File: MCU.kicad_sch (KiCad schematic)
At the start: 48 parts, among them IC3 TCAN330DCNT, J1 BM04B-GHS-TBT_LF__SN__N_, J2 Conn_01x04_Pin, J3 USB_C_Receptacle_USB2.0_16P, J4 BM04B-GHS-TBT_LF__SN__N_, J5 Conn_01x02_Socket, SW1 SW_SPDT, SW2 SW_SPDT, U2 STM32G431CBU6, U3 ME6211C33M5, Y1 ECS-80-20-5PX-TR

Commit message: all routed pcb
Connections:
- net I2C1_SCL: no longer J4.3, R22.2, U2.45 (PB7)
- new net I2C1_SDA: J4.3, R22.2, U2.45 (PB7)
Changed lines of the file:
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@@
-	)
-	(junction
-		(at 68.58 60.96)
-		(diameter 0)
-		(color 0 0 0 0)
 	)
 	(junction
@@
 	(wire
 		(pts
-			(xy 68.58 60.96) (xy 71.12 60.96)
+			(xy 45.72 60.96) (xy 71.12 60.96)
 		)
 		(stroke
@@
 		)
 		(stroke
-			(width 0)
-			(type default)
-		)
-	)
-	(wire
-		(pts
-			(xy 45.72 60.96) (xy 68.58 60.96)
-		)
-		(stroke

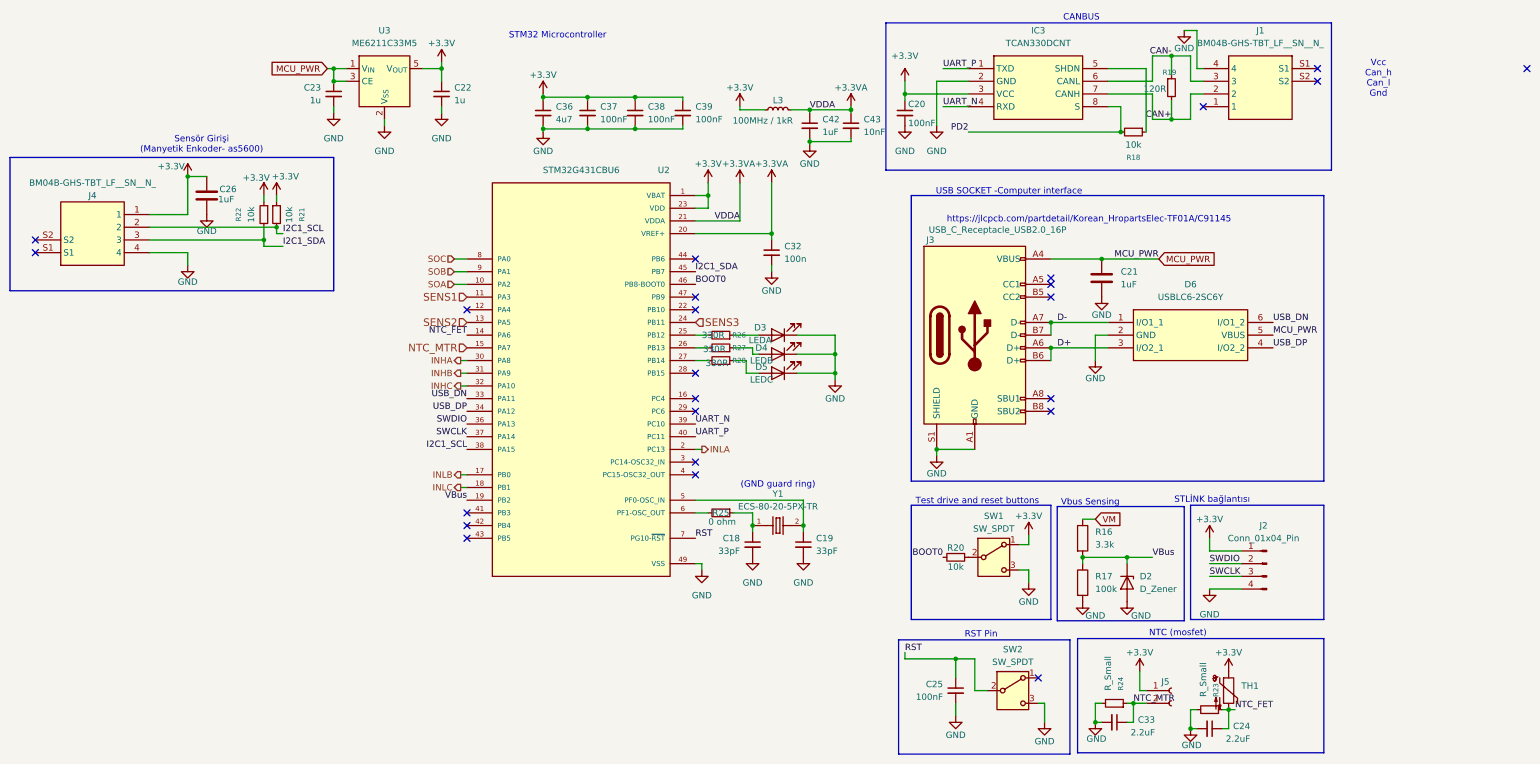
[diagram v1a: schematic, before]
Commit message: New one_GND_Layer pcb desgin has finished yet. DRC Rule checks needs to be controlling and correcting still.
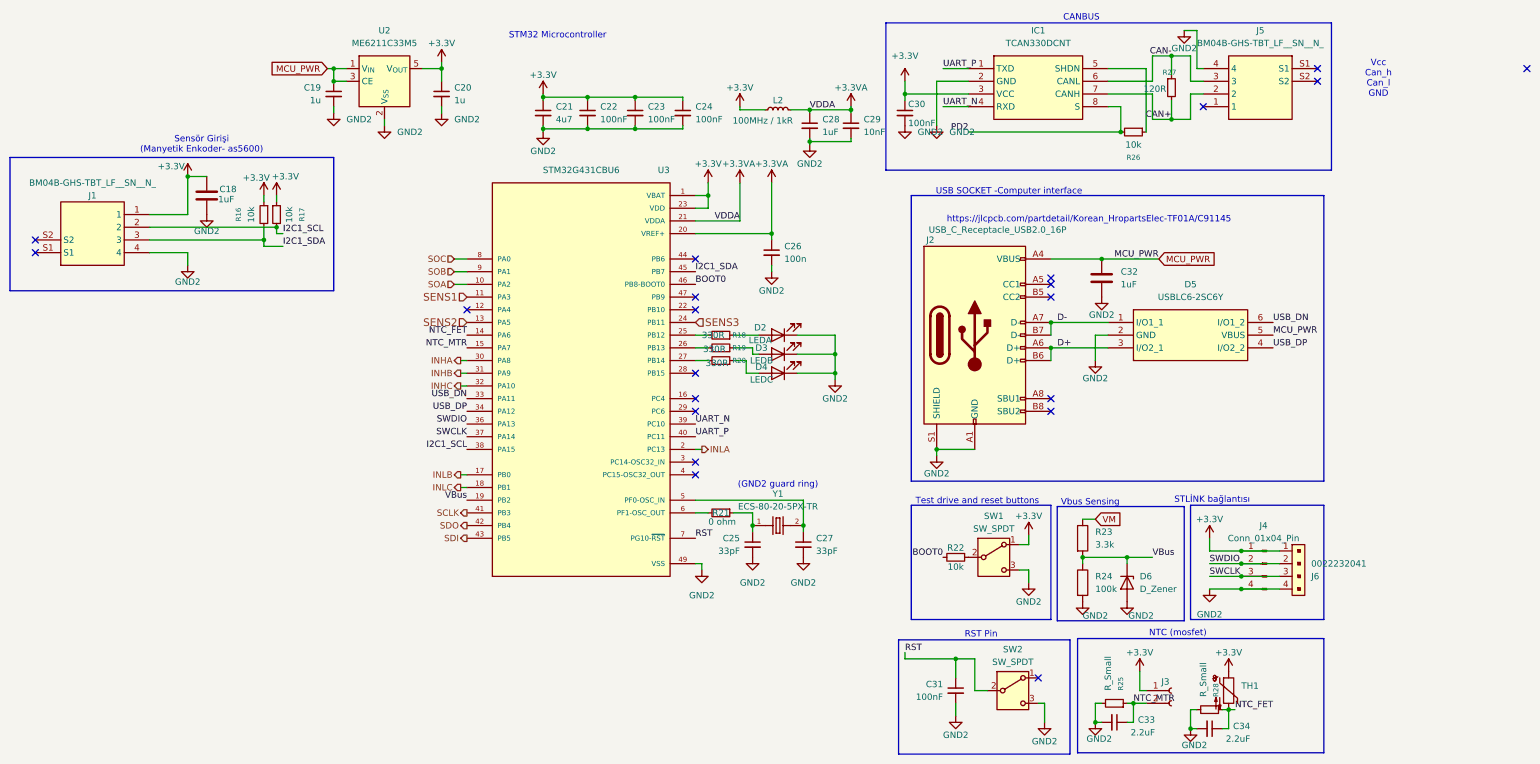
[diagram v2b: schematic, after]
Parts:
- added J6: 0022232041, digikey-footprints:PinHeader_1x4_P2.54mm_Drill1.02mm, symbol dk_Rectangular-Connectors-Headers-Male-Pins:0022232041
- renumbered C26 to C18, C23 to C19, C22 to C20, C36 to C21, C37 to C22, C38 to C23, C39 to C24, C18 to C25, C32 to C26, C19 to C27, C42 to C28, C43 to C29, C20 to C30, C25 to C31, C21 to C32, C24 to C34, D3 to D2, D4 to D3, D5 to D4, D6 to D5, D2 to D6, IC3 to IC1, J4 to J1, J3 to J2, J5 to J3, J2 to J4, J1 to J5, L3 to L2, R22 to R16, R21 to R17, R26 to R18, R27 to R19, R28 to R20, R25 to R21, R20 to R22, R16 to R23, R17 to R24, R24 to R25, R18 to R26, R19 to R27, R23 to R28, U3 to U2, U2 to U3
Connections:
- net +3.3V: now also J6.1
- net SWCLK: now also J6.3
- net SWDIO: now also J6.2
- net SCLK: now reaches U3.41 (PB3)
- net SDO: now reaches U3.42 (PB4)
- net SDI: now reaches U3.43 (PB5)
- net GND renamed GND2
- net GND2: now also J6.4
- no-connect marks 24 -> 21
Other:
- note added: "(GND2 guard ring)"
- note added: "Vcc Can_h Can_l GND"
- note removed: "(GND guard ring)"
- note removed: "Vcc Can_h Can_l Gnd"

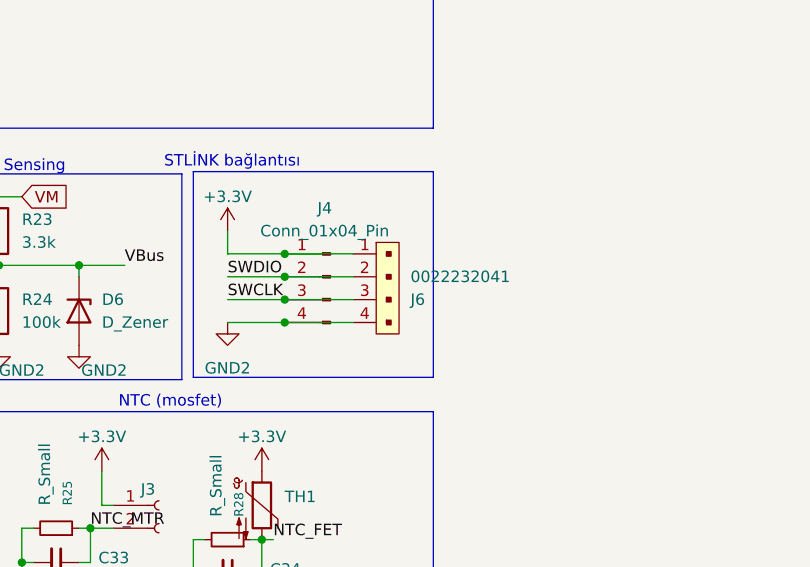
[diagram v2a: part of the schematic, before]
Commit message: some drc rule checks and correcting
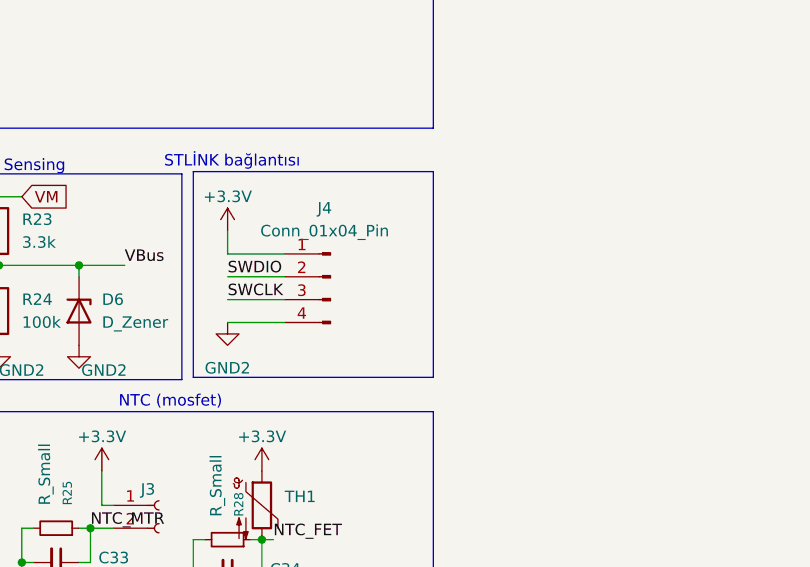
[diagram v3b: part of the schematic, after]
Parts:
- removed J6: 0022232041, digikey-footprints:PinHeader_1x4_P2.54mm_Drill1.02mm, symbol dk_Rectangular-Connectors-Headers-Male-Pins:0022232041
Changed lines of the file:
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@@
 	)
 	(junction
-		(at 264.16 125.73)
-		(diameter 0)
-		(color 0 0 0 0)
-	)
-	(junction
 		(at 196.85 34.29)
 		(diameter 0)
@@
 	)
 	(junction
-		(at 264.16 133.35)
-		(diameter 0)
-		(color 0 0 0 0)
-	)
-	(junction
 		(at 133.35 41.275)
 		(diameter 0)
@@
 	)
 	(junction
-		(at 264.16 130.81)
-		(diameter 0)
-		(color 0 0 0 0)
-	)
-	(junction
-		(at 264.16 128.27)
-		(diameter 0)
-		(color 0 0 0 0)
-	)
-	(junction
 		(at 166.37 120.65)
 		(diameter 0)
@@
 	(wire
 		(pts
-			(xy 264.16 133.35) (xy 271.78 133.35)
-		)
-		(stroke
-			(width 0)
-			(type default)
-		)
-	)
-	(wire
-		(pts
 			(xy 234.95 82.55) (xy 234.95 87.63)
 		)
@@
 	(wire
 		(pts
-			(xy 264.16 125.73) (xy 271.78 125.73)
-		)
-		(stroke
-			(width 0)
-			(type default)
-		)
-	)
-	(wire
-		(pts
 			(xy 170.18 62.23) (xy 170.18 63.5)
 		)
@@
 	(wire
 		(pts
-			(xy 264.16 128.27) (xy 271.78 128.27)
-		)
-		(stroke
-			(width 0)
-			(type default)
-		)
-	)
-	(wire
-		(pts
 			(xy 224.79 160.02) (xy 224.79 156.21)
 		)
@@
 	(wire
 		(pts
-			(xy 264.16 130.81) (xy 271.78 130.81)
-		)
-		(stroke
-			(width 0)
-			(type default)
-		)
-	)
-	(wire
-		(pts
 			(xy 124.46 41.275) (xy 133.35 41.275)
 		)
@@
 					(unit 1)
 				)
-			)
-		)
-	)
-	(symbol
-		(lib_id "dk_Rectangular-Connectors-Headers-Male-Pins:0022232041")
-		(at 274.32 125.73 90)
-		(mirror x)
-		(unit 1)
-		(exclude_from_sim no)
-		(in_bom yes)
-		(on_board yes)
-		(dnp no)
-		(property "Reference" "J6"
-			(at 278.13 130.8101 90)
-			(effects
-				(font
-					(size 1.27 1.27)
-				)
-				(justify right)
-			)
-		)
-		(property "Value" "0022232041"
-			(at 278.13 128.2701 90)
-			(effects
-				(font
-					(size 1.27 1.27)
-				)
-				(justify right)
-			)
-		)
-		(property "Footprint" "digikey-footprints:PinHeader_1x4_P2.54mm_Drill1.02mm"
-			(at 269.24 130.81 0)
-			(effects
-				(font
-					(size 1.524 1.524)
-				)
-				(justify left)
-				(hide yes)
-			)
-		)
-		(property "Datasheet" "https://www.molex.com/pdm_docs/sd/022232041_sd.pdf"
-			(at 266.7 130.81 0)
-			(effects
-				(font
-					(size 1.524 1.524)
-				)
-				(justify left)
-				(hide yes)
-			)
-		)
-		(property "Description" "CONN HEADER VERT 4POS 2.54MM"
-			(at 274.32 125.73 0)
-			(effects
-				(font
-					(size 1.27 1.27)
-				)
-				(hide yes)
-			)
-		)
-		(property "Digi-Key_PN" "WM4202-ND"
-			(at 264.16 130.81 0)
-			(effects
-				(font
-					(size 1.524 1.524)
-				)
-				(justify left)
-				(hide yes)
-			)
-		)
-		(property "MPN" "0022232041"
-			(at 261.62 130.81 0)
-			(effects
-				(font
-					(size 1.524 1.524)
-				)
-				(justify left)
-				(hide yes)
-			)
-		)
-		(property "Category" "Connectors, Interconnects"
-			(at 259.08 130.81 0)
-			(effects
-				(font
-					(size 1.524 1.524)
-				)
-				(justify left)
-				(hide yes)
-			)
-		)
-		(property "Family" "Rectangular Connectors - Headers, Male Pins"
-			(at 256.54 130.81 0)
-			(effects
-				(font
-					(size 1.524 1.524)
-				)
-				(justify left)
-				(hide yes)
-			)
-		)
-		(property "DK_Datasheet_Link" "https://www.molex.com/pdm_docs/sd/022232041_sd.pdf"
-			(at 254 130.81 0)
-			(effects
-				(font
-					(size 1.524 1.524)
-				)
-				(justify left)
-				(hide yes)
-			)
-		)
-		(property "DK_Detail_Page" "/product-detail/en/molex/0022232041/WM4202-ND/26671"
-			(at 251.46 130.81 0)
-			(effects
-				(font
-					(size 1.524 1.524)
-				)
-				(justify left)
-				(hide yes)
-			)
-		)
-		(property "Description_1" "CONN HEADER VERT 4POS 2.54MM"
-			(at 248.92 130.81 0)
-			(effects
-				(font
-					(size 1.524 1.524)
-				)
-				(justify left)
-				(hide yes)
-			)
-		)
-		(property "Manufacturer" "Molex"
-			(at 246.38 130.81 0)
-			(effects
-				(font
-					(size 1.524 1.524)
-				)
-				(justify left)
-				(hide yes)
-			)
-		)
-		(property "Status" "Active"
-			(at 243.84 130.81 0)
-			(effects
-				(font
-					(size 1.524 1.524)
-				)
-				(justify left)
-				(hide yes)
-			)
-		)
-		(pin "2"
-		)
-		(pin "1"
-		)
-		(pin "3"
-		)
-		(pin "4"
-		)
-		(instances
-			(project ""
-				(path "/57129761-6d47-486c-bd7a-90dbb6f75754/223db1af-68f5-46b9-9722-256b09606f21"
-					(reference "J6")
-					(unit 1)
-				)

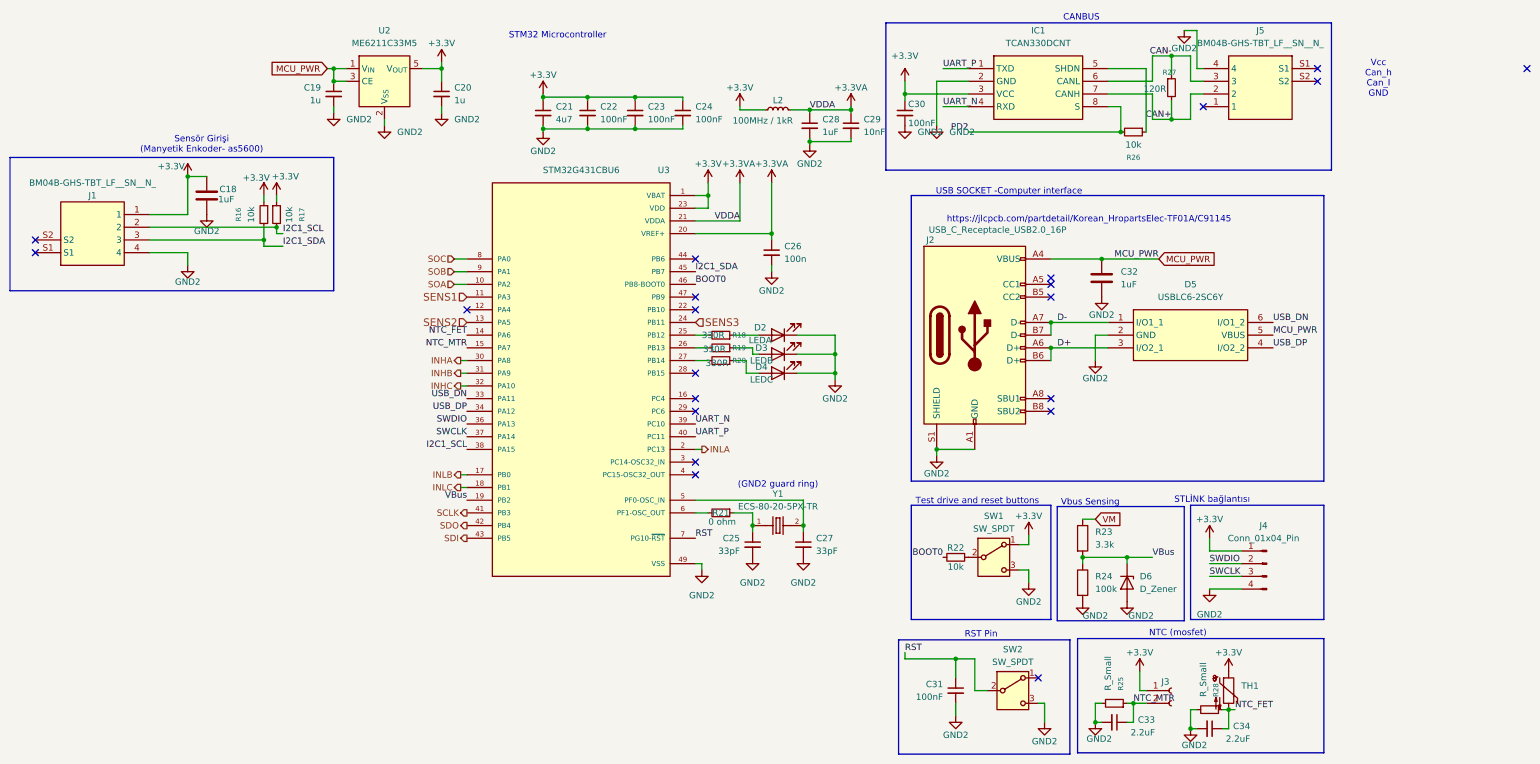
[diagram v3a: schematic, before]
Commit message: BOM list prepared for ekom and direnc.net
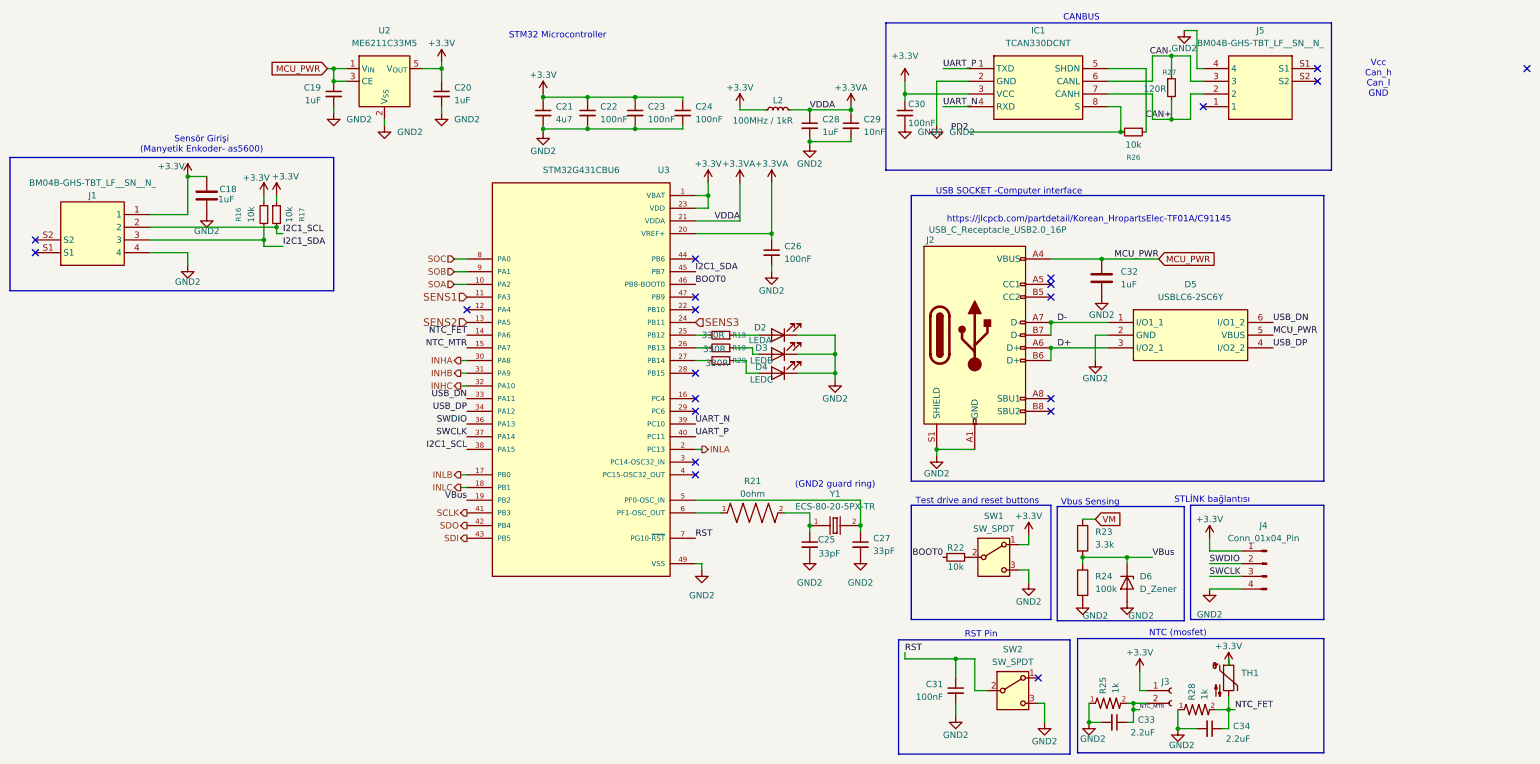
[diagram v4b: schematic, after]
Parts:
- removed R21: 0 ohm, RMCF0603ZT0R00:RESC1508X55N, symbol Device:R_Small
- removed R25, R28: R_Small, Resistor_SMD:R_0603_1608Metric_Pad0.98x0.95mm_HandSolder, symbol Device:R_Small
- added R21: 0ohm, RMCF0603ZT0R00:RESC1508X55N, symbol RMCF0603ZT0R00:RMCF0603ZT0R00
- added R25, R28: 1k, Resistor_SMD:R_0603_1608Metric_Pad0.98x0.95mm_HandSolder, symbol RNCP0603FTD1K00:RNCP0603FTD1K00
- C18, C32, C33, C34: footprint Capacitor_SMD:C_0603_1608Metric -> Capacitor_SMD:C_0603_1608Metric_Pad1.08x0.95mm_HandSolder
- C19, C20: value 1u -> 1uF
- C22, C23, C24, C30: footprint Capacitor_SMD:C_0603_1608Metric_Pad1.08x0.95mm_HandSolder -> Capacitor_SMD:C_0805_2012Metric_Pad1.18x1.45mm_HandSolder
- C26: value 100n -> 100nF; footprint Capacitor_SMD:C_0603_1608Metric_Pad1.08x0.95mm_HandSolder -> Capacitor_SMD:C_0805_2012Metric_Pad1.18x1.45mm_HandSolder
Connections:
- net GND2: now also R25.1, R28.1
- net NTC_FET: now also R28.2
- net NTC_MTR: now also R25.2
- net at C25.1, Y1.1: now also R21.2
- net at U3.6 (PF1-OSC_OUT): now also R21.1
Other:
- moved on the sheet: C25, C27, TH1, Y1

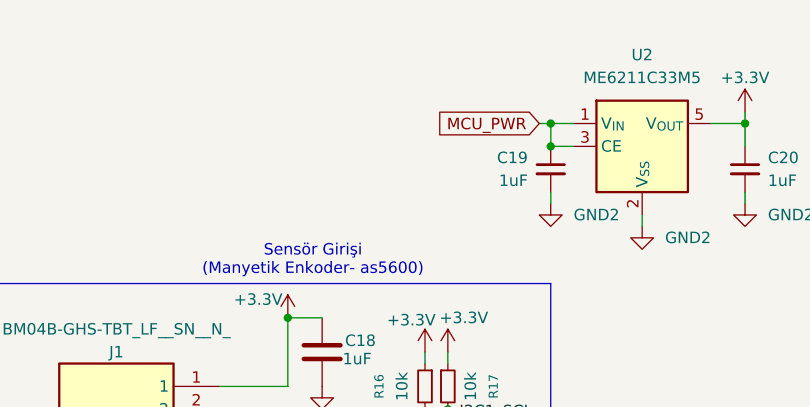
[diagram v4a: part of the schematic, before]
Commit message: for LCSC components the layout/footprints changed. Previous commit for ekom/direncnet components.
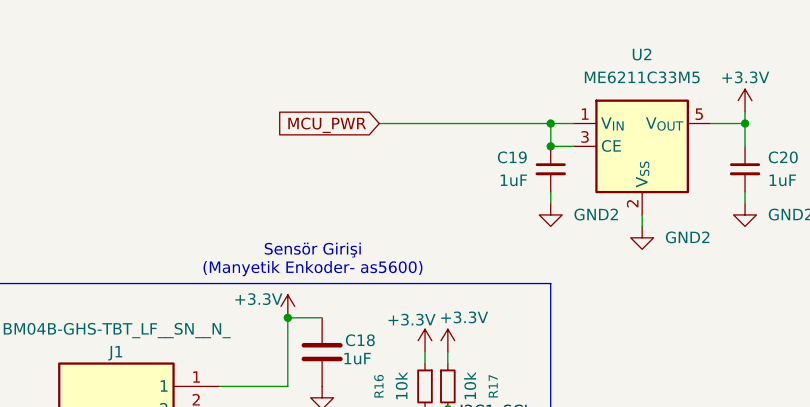
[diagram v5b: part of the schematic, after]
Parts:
- C22, C23, C24, C25, C26, C27, C30, C31: footprint Capacitor_SMD:C_0805_2012Metric_Pad1.18x1.45mm_HandSolder -> Capacitor_SMD:C_0603_1608Metric_Pad1.08x0.95mm_HandSolder
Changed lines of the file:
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@@
 	(wire
 		(pts
-			(xy 81.28 29.21) (xy 82.55 29.21)
+			(xy 63.5 29.21) (xy 82.55 29.21)
 		)
 		(stroke
@@
 	(global_label "MCU_PWR"
 		(shape input)
-		(at 81.28 29.21 180)
+		(at 63.5 29.21 180)
 		(fields_autoplaced yes)
 		(effects
@@
 		)
 		(property "Intersheetrefs" "${INTERSHEET_REFS}"
-			(at 69.2839 29.21 0)
+			(at 51.5039 29.21 0)
 			(effects
 				(font
@@
 			)
 		)
-		(property "Footprint" "Capacitor_SMD:C_0805_2012Metric_Pad1.18x1.45mm_HandSolder"
+		(property "Footprint" "Capacitor_SMD:C_0603_1608Metric_Pad1.08x0.95mm_HandSolder"
 			(at 207.01 153.67 0)
 			(effects
@@
 			)
 		)
-		(property "Footprint" "Capacitor_SMD:C_0805_2012Metric_Pad1.18x1.45mm_HandSolder"
+		(property "Footprint" "Capacitor_SMD:C_0603_1608Metric_Pad1.08x0.95mm_HandSolder"
 			(at 152.4 38.1 0)
 			(effects
@@
 			)
 		)
-		(property "Footprint" "Capacitor_SMD:C_0805_2012Metric_Pad1.18x1.45mm_HandSolder"
+		(property "Footprint" "Capacitor_SMD:C_0603_1608Metric_Pad1.08x0.95mm_HandSolder"
 			(at 196.85 38.1 0)
 			(effects
@@
 			)
 		)
-		(property "Footprint" "Capacitor_SMD:C_0805_2012Metric_Pad1.18x1.45mm_HandSolder"
+		(property "Footprint" "Capacitor_SMD:C_0603_1608Metric_Pad1.08x0.95mm_HandSolder"
 			(at 170.18 66.04 0)
 			(effects
@@
 			)
 		)
-		(property "Footprint" "Capacitor_SMD:C_0805_2012Metric_Pad1.18x1.45mm_HandSolder"
+		(property "Footprint" "Capacitor_SMD:C_0603_1608Metric_Pad1.08x0.95mm_HandSolder"
 			(at 142.875 38.1 0)
 			(effects
@@
 			)
 		)
-		(property "Footprint" "Capacitor_SMD:C_0805_2012Metric_Pad1.18x1.45mm_HandSolder"
+		(property "Footprint" "Capacitor_SMD:C_0603_1608Metric_Pad1.08x0.95mm_HandSolder"
 			(at 187.96 124.46 0)
 			(effects
@@
 			)
 		)
-		(property "Footprint" "Capacitor_SMD:C_0805_2012Metric_Pad1.18x1.45mm_HandSolder"
+		(property "Footprint" "Capacitor_SMD:C_0603_1608Metric_Pad1.08x0.95mm_HandSolder"
 			(at 133.35 38.1 0)
 			(effects
@@
 			)
 		)
-		(property "Footprint" "Capacitor_SMD:C_0805_2012Metric_Pad1.18x1.45mm_HandSolder"
+		(property "Footprint" "Capacitor_SMD:C_0603_1608Metric_Pad1.08x0.95mm_HandSolder"
 			(at 177.8 124.46 0)
 			(effects
